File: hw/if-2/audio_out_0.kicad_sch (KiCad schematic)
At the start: 18 parts, among them U81 TL072

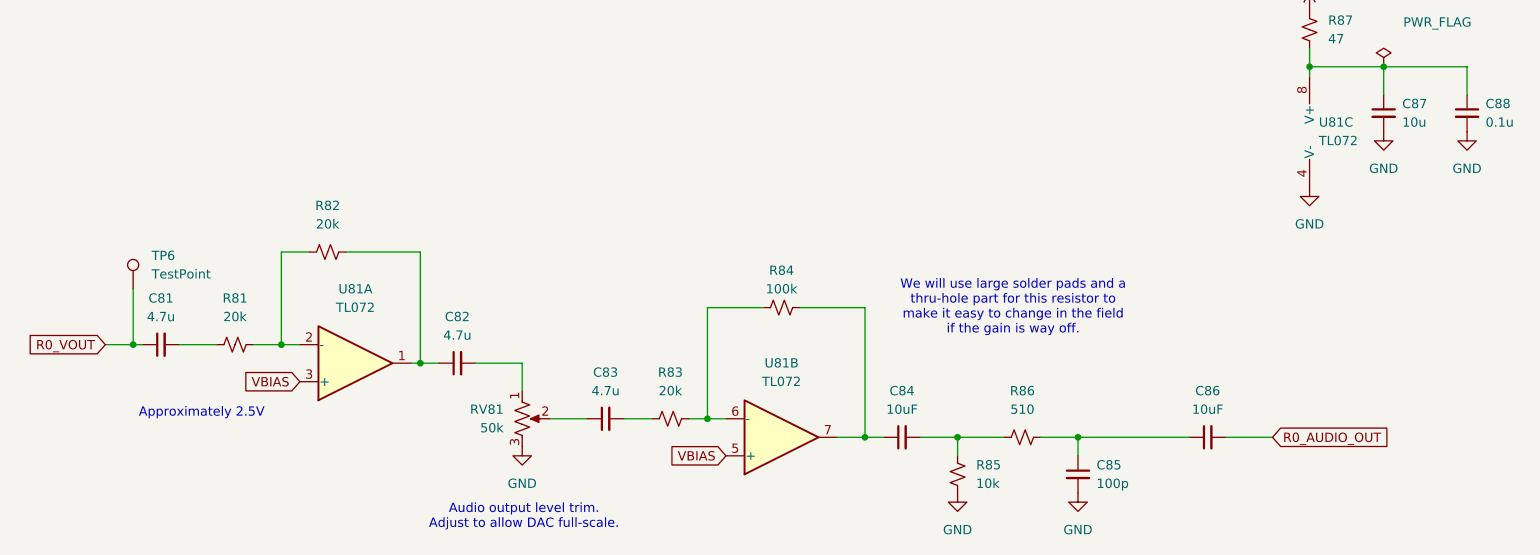
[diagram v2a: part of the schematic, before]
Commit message: Updated audio file to 16K
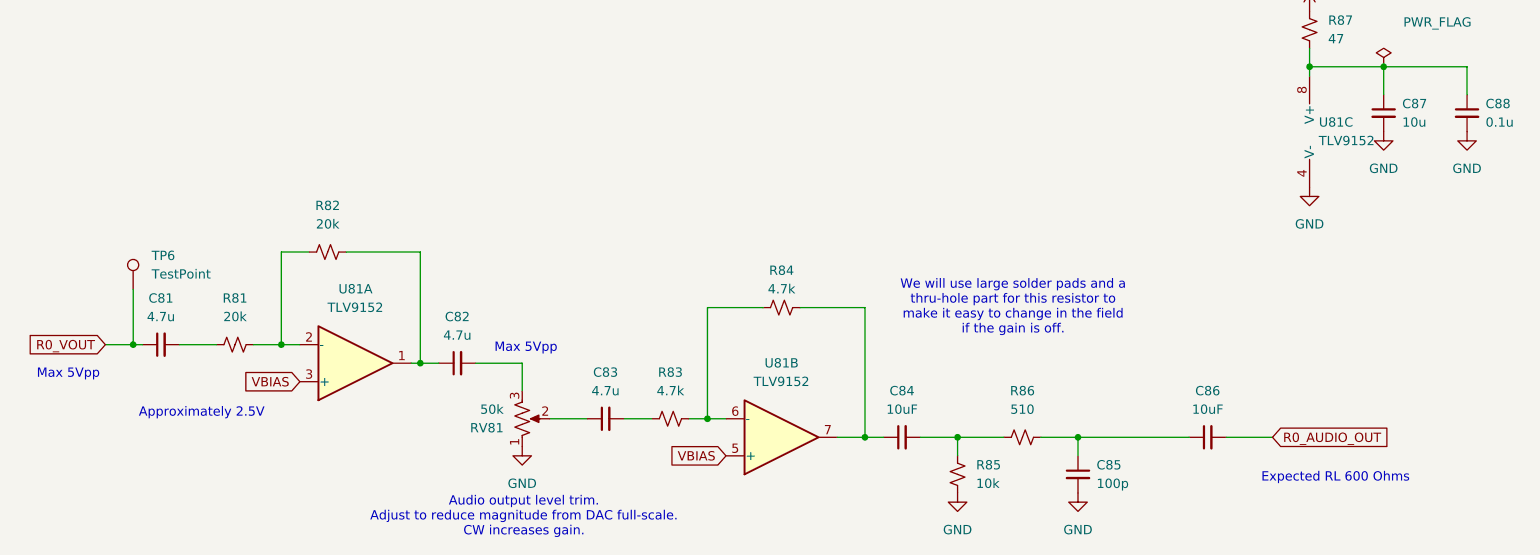
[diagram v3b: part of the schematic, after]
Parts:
- R83: value 20k -> 4.7k
- R84: value 100k -> 4.7k
- U81: value TL072 -> TLV9152
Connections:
- net GND: now also RV81.1; no longer RV81.3
- net at C82.2: now also RV81.3; no longer RV81.1
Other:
- note added: "Audio output level trim. Adjust to reduce magnitude from DAC full-scale. CW increases gain."
- note added: "Expected RL 600 Ohms"
- note added: "Max 5Vpp"
- note added: "We will use large solder pads and a thru-hole part for this resistor to make it easy to change in the field if the gain is off."
- note removed: "Audio output level trim. Adjust to allow DAC full-scale."
- note removed: "We will use large solder pads and a thru-hole part for this resistor to make it easy to change in the field if the gain is way off."
- title: COS/CTCSS/PTT Controls (Radio 0) -> Audio Output (Radio 0)
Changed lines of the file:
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@@
 	(paper "USLetter")
 	(title_block
-		(title "COS/CTCSS/PTT Controls (Radio 0)")
+		(title "Audio Output (Radio 0)")
 		(date "2025-06-21")
 		(rev "3")
@@
 		(comment 2 "NOT FOR COMMERCIAL USE")
 	)
+	(text "Max 5Vpp"
+		(exclude_from_sim no)
+		(at 58.42 77.724 0)
+		(effects
+			(font
+				(size 1.27 1.27)
+				(color 254 69 255 1)
+			)
+		)
+	)
+	(text "Expected RL 600 Ohms"
+		(exclude_from_sim no)
+		(at 232.156 91.948 0)
+		(effects
+			(font
+				(size 1.27 1.27)
+				(color 254 69 255 1)
+			)
+		)
+	)
 	(text "Approximately 2.5V\n"
 		(exclude_from_sim no)
@@
 		)
 	)
-	(text "We will use large solder pads and a \nthru-hole part for this resistor to \nmake it easy to change in the field\nif the gain is way off."
+	(text "We will use large solder pads and a \nthru-hole part for this resistor to \nmake it easy to change in the field\nif the gain is off."
 		(exclude_from_sim no)
 		(at 187.96 68.58 0)
@@
 		)
 	)
-	(text "Audio output level trim.\nAdjust to allow DAC full-scale.\n"
+	(text "Audio output level trim.\nAdjust to reduce magnitude from DAC full-scale.\nCW increases gain."
 		(exclude_from_sim no)
 		(at 120.904 97.282 0)
@@
 		)
 	)
+	(text "Max 5Vpp"
+		(exclude_from_sim no)
+		(at 121.158 74.168 0)
+		(effects
+			(font
+				(size 1.27 1.27)
+				(color 254 69 255 1)
+			)
+		)
+	)
 	(junction
 		(at 167.64 86.36)
@@
 			)
 		)
-		(property "Value" "TL072"
+		(property "Value" "TLV9152"
 			(at 229.87 45.7199 0)
 			(effects
@@
 		(lib_id "Device:R_Potentiometer_US")
 		(at 120.65 83.82 0)
-		(unit 1)
-		(exclude_from_sim no)
-		(in_bom yes)
-		(on_board yes)
-		(dnp no)
-		(fields_autoplaced yes)
+		(mirror x)
+		(unit 1)
+		(exclude_from_sim no)
+		(in_bom yes)
+		(on_board yes)
+		(dnp no)
 		(property "Reference" "RV81"
-			(at 118.11 82.5499 0)
+			(at 118.11 85.0901 0)
 			(effects
 				(font
@@
 		)
 		(property "Value" "50k"
-			(at 118.11 85.0899 0)
+			(at 118.11 82.5501 0)
 			(effects
 				(font
@@
 			)
 		)
-		(property "Value" "TL072"
+		(property "Value" "TLV9152"
 			(at 156.21 78.74 0)
 			(effects
@@
 			)
 		)
-		(property "Value" "20k"
+		(property "Value" "4.7k"
 			(at 140.97 80.01 90)
 			(effects
@@
 			)
 		)
-		(property "Value" "TL072"
+		(property "Value" "TLV9152"
 			(at 97.79 68.58 0)
 			(effects
@@
 			)
 		)
-		(property "Value" "100k"
+		(property "Value" "4.7k"
 			(at 156.21 66.04 90)
 			(effects

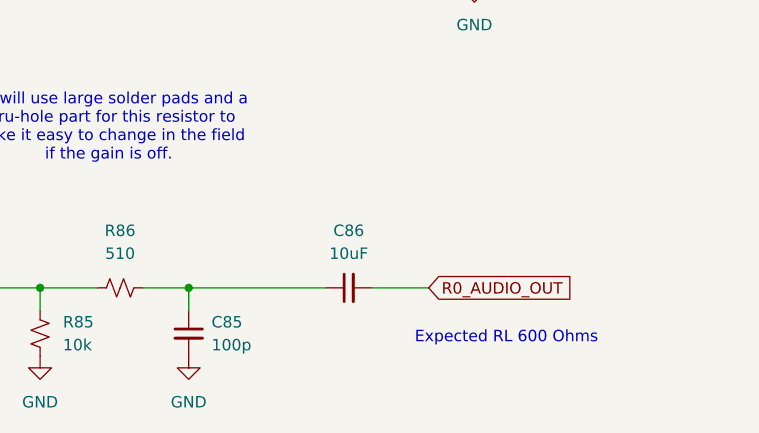
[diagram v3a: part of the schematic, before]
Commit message: Updating schematics, create new mini-board for radio interface
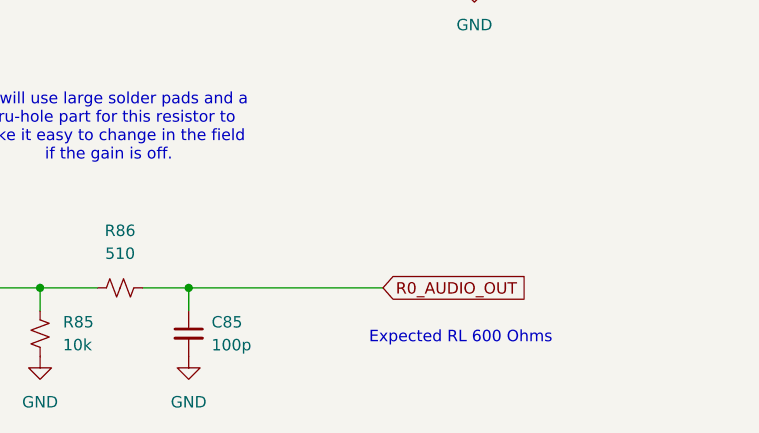
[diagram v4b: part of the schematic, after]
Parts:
- removed C86: 10uF, Capacitor_SMD:C_0805_2012Metric_Pad1.18x1.45mm_HandSolder, symbol Device:C_Small
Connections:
- net R0_AUDIO_OUT: now also C85.1, R86.2
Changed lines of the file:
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@@
 	(text "Expected RL 600 Ohms"
 		(exclude_from_sim no)
-		(at 232.156 91.948 0)
+		(at 227.076 91.948 0)
 		(effects
 			(font
@@
 	(wire
 		(pts
-			(xy 196.85 86.36) (xy 212.09 86.36)
+			(xy 196.85 86.36) (xy 218.44 86.36)
 		)
 		(stroke
@@
 		(pts
 			(xy 106.68 76.2) (xy 109.22 76.2)
-		)
-		(stroke
-			(width 0)
-			(type default)
-		)
-	)
-	(wire
-		(pts
-			(xy 217.17 86.36) (xy 223.52 86.36)
 		)
 		(stroke
@@
 	(global_label "R0_AUDIO_OUT"
 		(shape input)
-		(at 223.52 86.36 0)
+		(at 218.44 86.36 0)
 		(fields_autoplaced yes)
 		(effects
@@
 		)
 		(property "Intersheetrefs" "${INTERSHEET_REFS}"
-			(at 240.1729 86.36 0)
+			(at 235.0929 86.36 0)
 			(effects
 				(font
@@
 					(unit 1)
 				)
-			)
-		)
-	)
-	(symbol
-		(lib_id "Device:C_Small")
-		(at 214.63 86.36 90)
-		(unit 1)
-		(exclude_from_sim no)
-		(in_bom yes)
-		(on_board yes)
-		(dnp no)
-		(fields_autoplaced yes)
-		(property "Reference" "C86"
-			(at 214.6363 80.01 90)
-			(effects
-				(font
-					(size 1.27 1.27)
-				)
-			)
-		)
-		(property "Value" "10uF"
-			(at 214.6363 82.55 90)
-			(effects
-				(font
-					(size 1.27 1.27)
-				)
-			)
-		)
-		(property "Footprint" "Capacitor_SMD:C_0805_2012Metric_Pad1.18x1.45mm_HandSolder"
-			(at 214.63 86.36 0)
-			(effects
-				(font
-					(size 1.27 1.27)
-				)
-				(hide yes)
-			)
-		)
-		(property "Datasheet" "~"
-			(at 214.63 86.36 0)
-			(effects
-				(font
-					(size 1.27 1.27)
-				)
-				(hide yes)
-			)
-		)
-		(property "Description" "Unpolarized capacitor, small symbol"
-			(at 214.63 86.36 0)
-			(effects
-				(font
-					(size 1.27 1.27)
-				)
-				(hide yes)
-			)
-		)
-		(pin "1"
-		)
-		(pin "2"
-		)
-		(instances
-			(project "if-2"
-				(path "/a8c2d6aa-29bb-49bd-a367-0d62a0a32480/44344ba6-1370-4a77-ab96-dbf60268a0b4"
-					(reference "C86")
-					(unit 1)
-				)

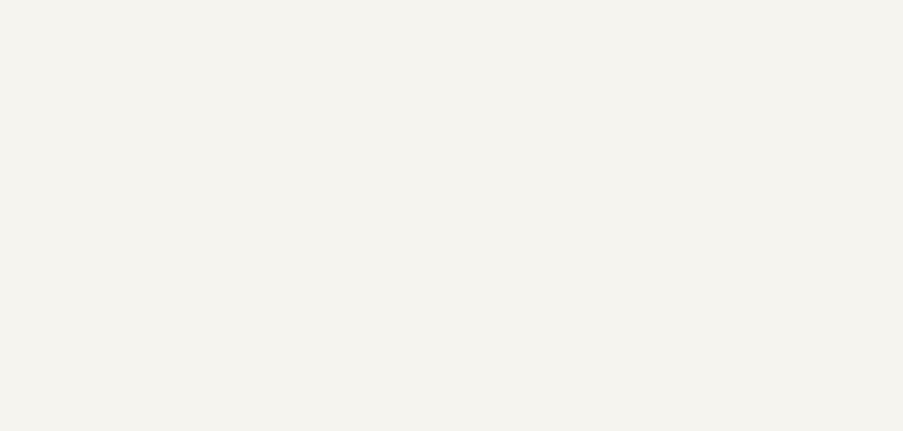
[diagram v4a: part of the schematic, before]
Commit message: Updating schematics, create new mini-board for radio interface
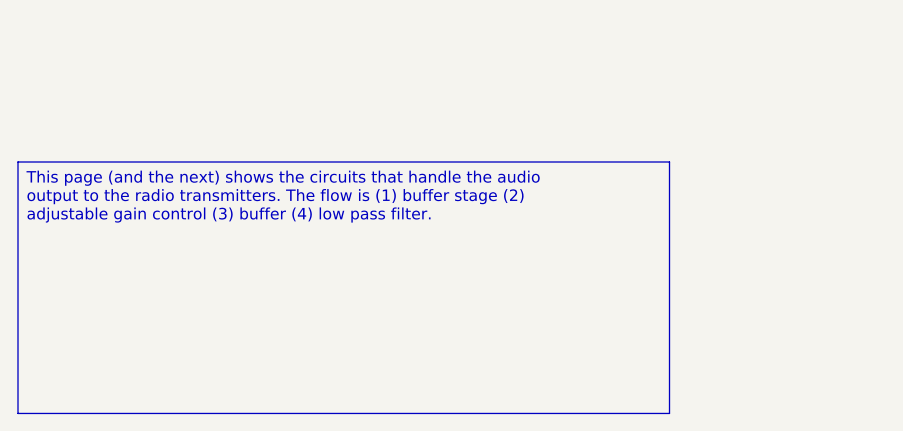
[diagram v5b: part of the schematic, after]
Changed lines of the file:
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@@
+		)
+	)
+	(text_box "This page (and the next) shows the circuits that handle the audio output to the radio transmitters. The flow is (1) buffer stage (2) adjustable gain control (3) buffer (4) low pass filter.\n"
+		(exclude_from_sim no)
+		(at 15.24 170.18 0)
+		(size 72.39 27.94)
+		(margins 0.9525 0.9525 0.9525 0.9525)
+		(stroke
+			(width 0)
+			(type solid)
+		)
+		(fill
+			(type color)
+			(color 205 245 255 1)
+		)
+		(effects
+			(font
+				(size 1.27 1.27)
+			)
+			(justify left top)
 		)
 	)
